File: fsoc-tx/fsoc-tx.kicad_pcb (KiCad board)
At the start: 4 copper layers, 52 x 45 mm, 52 parts, among them J1 USB4105-GF-A, J2 B8B-PH-K-S, J3 FTSH-105-01-L-DV-K, J4 B3B-PH-K-S, J5 Conn_01x03, SW1 SW_RESET, SW2 USB_BOOT, SW3 SW_DPST, U1 USBLC6-2SC6, U2 AP2112K-3.3, U3 RP2354A, U4 74AHCT1G125, U5 TPS22919DCK, Y1 ABM8-272-T3, Y2 ASTX-H11-10.000MHz-T

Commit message: TX PCB: checkpoint (almost finsihed)
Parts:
- moved SW1 51.5 mm to (155.0, 118.5), turned to 90 degrees
- moved J3 48.7 mm to (154.5, 131.0), turned to 180 degrees
- moved C21 38.2 mm to (115.5, 119.5), turned to 90 degrees
- moved R8 38.0 mm to (113.5, 119.5), turned to -90 degrees
- moved U4 35.6 mm to (116.0, 116.0), turned to 0 degrees
- moved R11 27.9 mm to (123.0, 122.5), turned to 180 degrees
- moved R9 27.6 mm to (121.5, 115.0), turned to 0 degrees
- moved J1 25.0 mm to (158.0, 106.0), turned to 90 degrees
- moved C11 21.0 mm to (126.0, 142.5), turned to 90 degrees
- moved R1 19.9 mm to (149.0, 110.5)
- moved C22 19.7 mm to (109.5, 134.0), turned to -90 degrees
- moved J4 19.2 mm to (120.0, 126.0)
- moved R13 17.9 mm to (109.5, 123.0), turned to -90 degrees
- moved R12 17.4 mm to (109.5, 119.0), turned to 90 degrees
- moved U5 15.8 mm to (114.5, 134.5), turned to 90 degrees
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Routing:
- net /+3V3_DIG: track 23.9 -> 171.1 mm, vias 0 -> 2
- net GND: track 14.6 -> 100.0 mm, vias 10 -> 51
- net /SYS_5V: track 0.00 -> 76.8 mm, vias 0 -> 3
- net /PPS_OUT: track 0.00 -> 59.4 mm
- net /HOST_READY: track 0.00 -> 58.3 mm
- net /TX_POWER_USB/VBUS_USB: track 0.00 -> 54.8 mm
- net /TX_LASER/LASER_MODULE_5V: track 0.00 -> 42.3 mm
- net Net-(R8-Pad2): track 0.00 -> 37.5 mm
- net /HOST_I2C_SCL: track 0.00 -> 37.3 mm
- net /HOST_I2C_SDA: track 0.00 -> 35.8 mm
- net /TX_MCU_CLOCK/RUN_N: track 0.00 -> 34.2 mm
- net /LASER_PWR_EN: track 0.00 -> 34.0 mm
- net /HOST_UART_RX: track 0.00 -> 32.9 mm
- net /TX_MCU_CLOCK/SWCLK: track 0.00 -> 32.7 mm
- net /HOST_UART_TX: track 0.00 -> 31.4 mm
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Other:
- board size 52 x 45 mm -> 61.5 x 45 mm

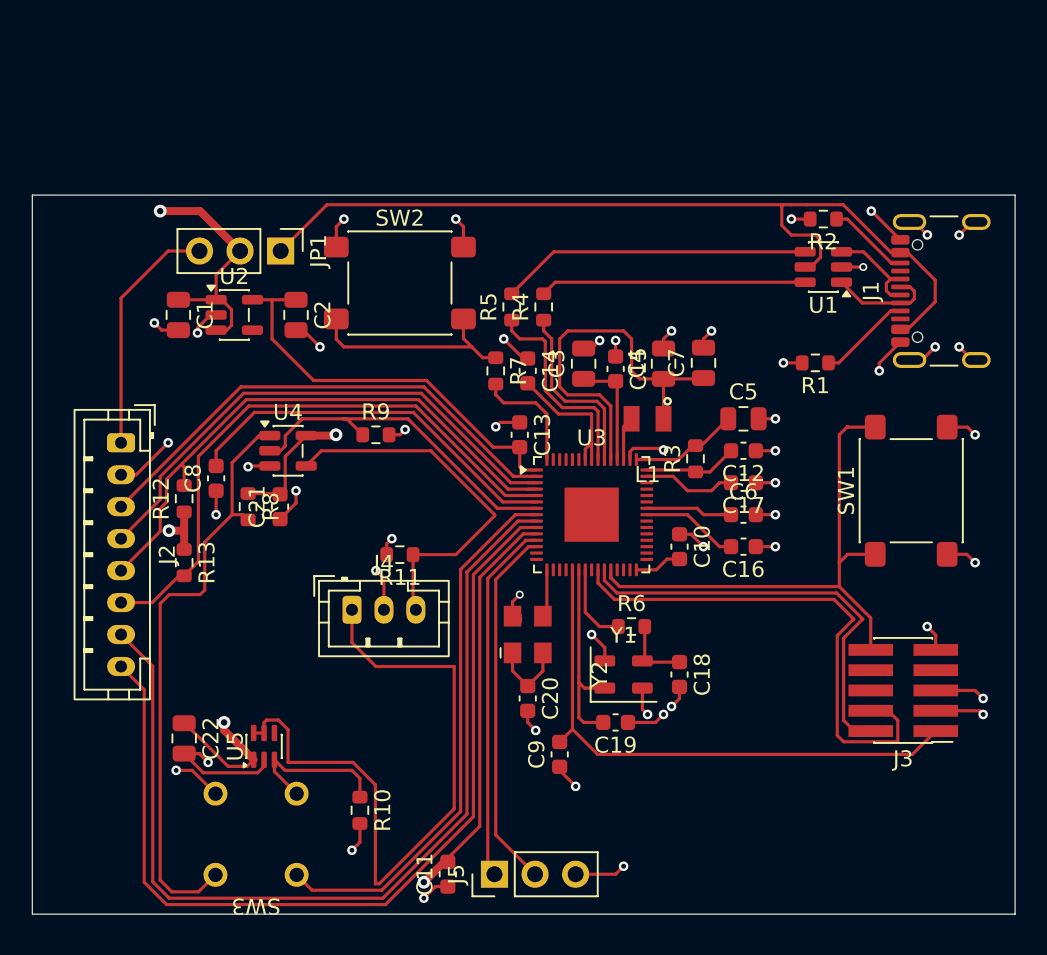
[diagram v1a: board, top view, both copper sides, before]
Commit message: TX PCB: checkpoint (error: non-plated through holes of GCT USB4105 has 0.194mm distance of the copper pads while the board steup is set to 0.25mm.. waiting approval)
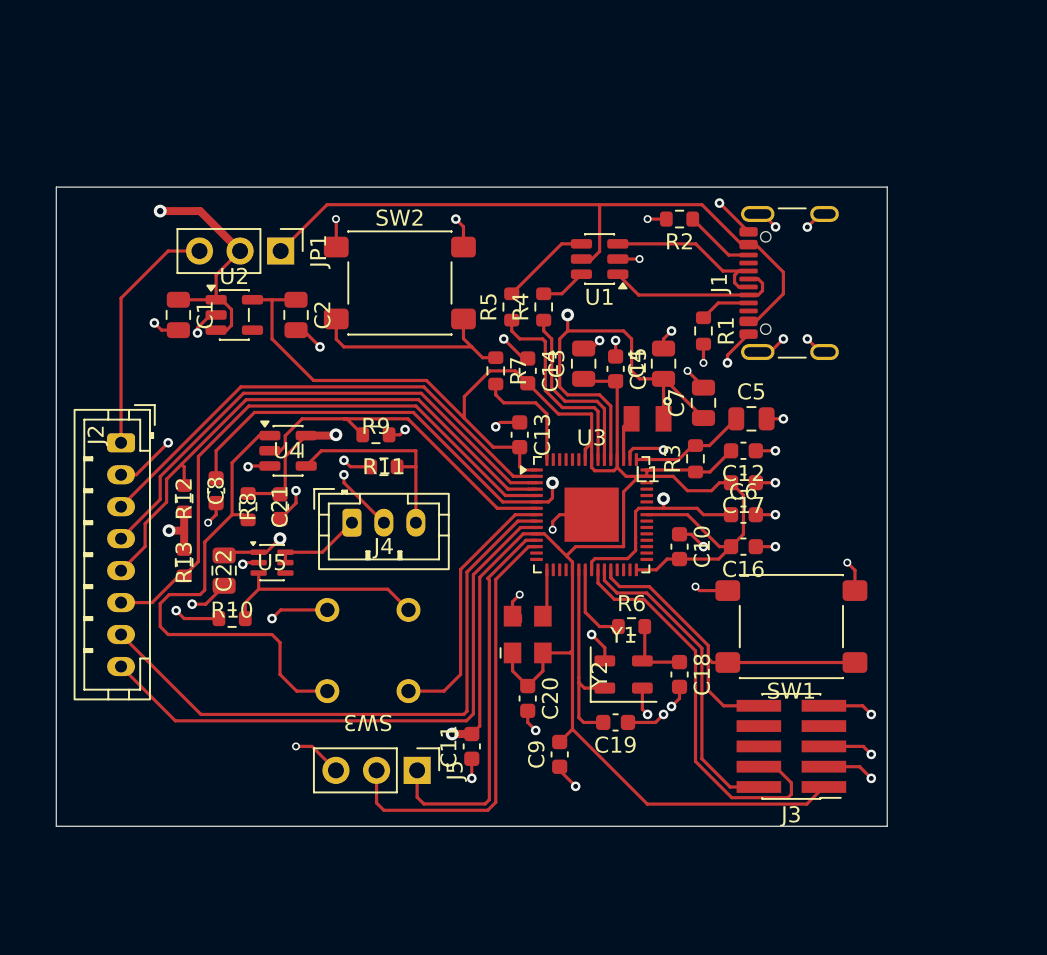
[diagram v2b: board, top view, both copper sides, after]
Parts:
- moved R10 14.4 mm to (112.5, 126.5), turned to 180 degrees
- moved U1 14.0 mm to (135.5, 104.0)
- moved SW3 13.5 mm to (121.0, 128.5)
- moved U5 11.5 mm to (115.0, 123.0), turned to 0 degrees
- moved SW1 11.3 mm to (147.5, 127.0), turned to 180 degrees
- moved C22 10.8 mm to (112.0, 123.5)
- moved J1 9.51 mm to (148.5, 105.5)
- moved R2 9.00 mm to (140.5, 101.5)
- moved C11 8.14 mm to (127.5, 134.5)
- moved J5 8.10 mm to (124.1, 136.0), turned to -90 degrees
- moved J3 7.83 mm to (147.5, 134.5)
- moved R1 7.28 mm to (142.0, 108.5), turned to -90 degrees
- moved R11 5.59 mm to (122.0, 117.0)
- moved J4 5.45 mm to (120.0, 120.5)
- moved C7 2.50 mm to (142.0, 113.0)
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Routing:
- net /TX_LASER/LASER_MODULE_5V: track 42.3 -> 5.58 mm
- net /TX_MCU_CLOCK/+1V1: track 54.3 -> 84.1 mm, vias 0 -> 3
- net /PPS_OUT: track 59.4 -> 38.2 mm
- net /HOST_READY: track 58.3 -> 38.0 mm
- net /LASER_PWR_EN: track 34.0 -> 16.4 mm
- net /SYS_5V: track 76.8 -> 59.7 mm
- net /USB_DM: track 16.7 -> 2.87 mm
- net /USB_DP: track 19.4 -> 5.66 mm
- net /TX_POWER_USB/VBUS_USB: track 54.8 -> 42.9 mm
- net /TX_LASER/LASER_DATA_5V: track 23.6 -> 12.9 mm
- net /TX_MCU_CLOCK/RUN_N: track 34.2 -> 24.0 mm
- net /+3V3_DIG: track 171.1 -> 180.2 mm
- net /TX_MCU_CLOCK/SWDIO: track 26.6 -> 19.7 mm
- net /TX_MCU_CLOCK/SWCLK: track 32.7 -> 25.8 mm
- net Net-(R8-Pad2): track 37.5 -> 30.8 mm
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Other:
- board size 61.5 x 45 mm -> 52 x 40 mm
